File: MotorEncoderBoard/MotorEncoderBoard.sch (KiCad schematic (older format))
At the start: 11 parts, among them P1 CONN_01X02, P2 CONN_01X02, U1 RPI-579N1, U2 LM311N

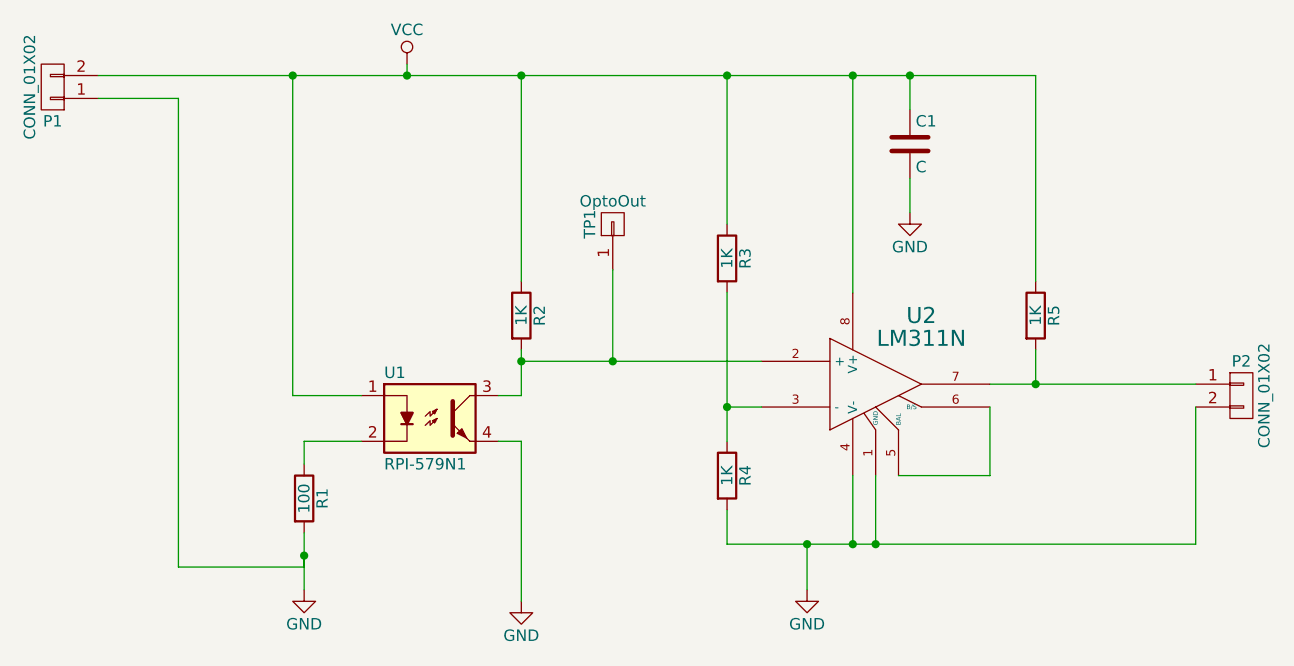
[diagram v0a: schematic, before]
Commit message: Updated schematic with MPNs and Links
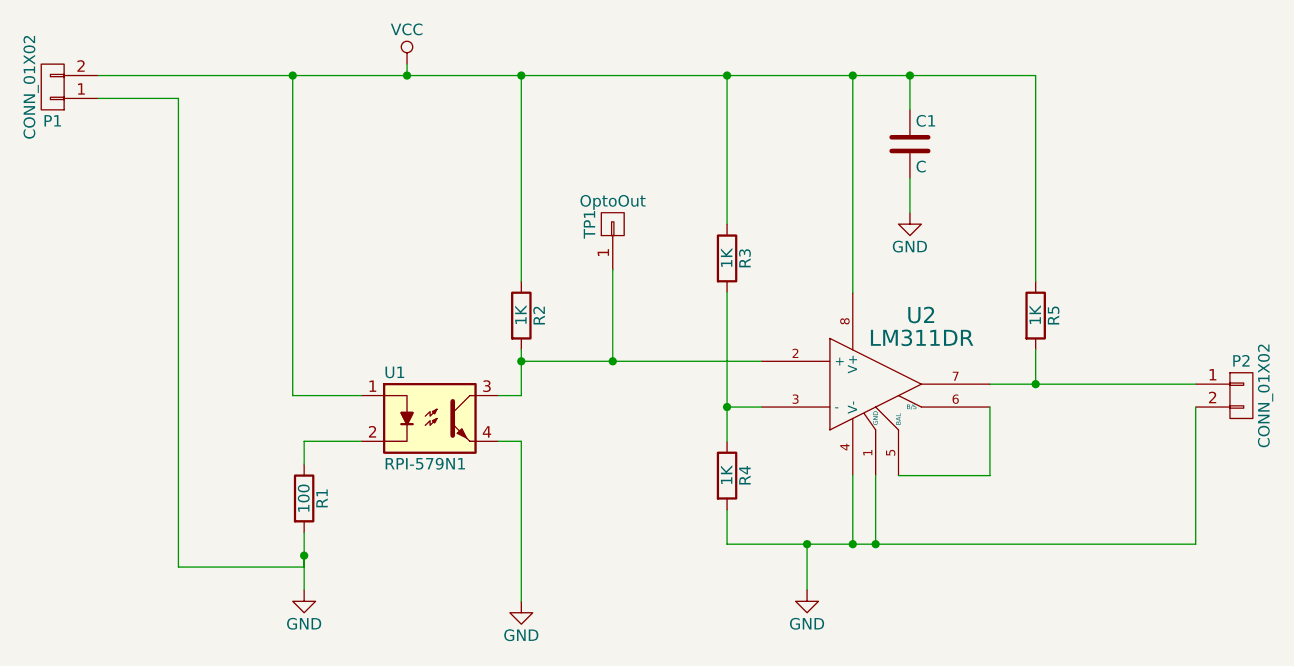
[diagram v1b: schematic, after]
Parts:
- U1: Link (none) -> http://parts.io/detail/710702/RPI-579N1; MPN (none) -> RPI-579N1
- U2: value LM311N -> LM311DR; Link (none) -> http://parts.io/detail/916052/LM311DR; MPN (none) -> LM311DR
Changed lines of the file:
@@
 F 2 "MotorEncoder:RPI-579N1" H 5750 3550 50  0001 L CIN
 F 3 "" H 5750 3250 50  0000 L CNN
+F 4 "RPI-579N1" H 5750 3350 60  0001 C CNN "MPN"
+F 5 "http://parts.io/detail/710702/RPI-579N1" H 5750 3350 60  0001 C CNN "Link"
 	1    5750 3350
 	1    0    0    -1
@@
 P 7700 3200
 F 0 "U2" H 7900 3500 70  0000 C CNN
-F 1 "LM311N" H 7900 3400 70  0000 C CNN
+F 1 "LM311DR" H 7900 3400 70  0000 C CNN
 F 2 "Housings_SOIC:SOIC-8_3.9x4.9mm_Pitch1.27mm" H 7700 3200 60  0001 C CNN
 F 3 "" H 7700 3200 60  0000 C CNN
+F 4 "LM311DR" H 7700 3200 60  0001 C CNN "MPN"
+F 5 "http://parts.io/detail/916052/LM311DR" H 7700 3200 60  0001 C CNN "Link"
 	1    7700 3200
 	1    0    0    -1
